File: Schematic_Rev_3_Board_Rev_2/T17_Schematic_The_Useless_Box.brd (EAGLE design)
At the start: 100 x 80 mm, 18 parts, among them U1 ATMEGA328P-AU

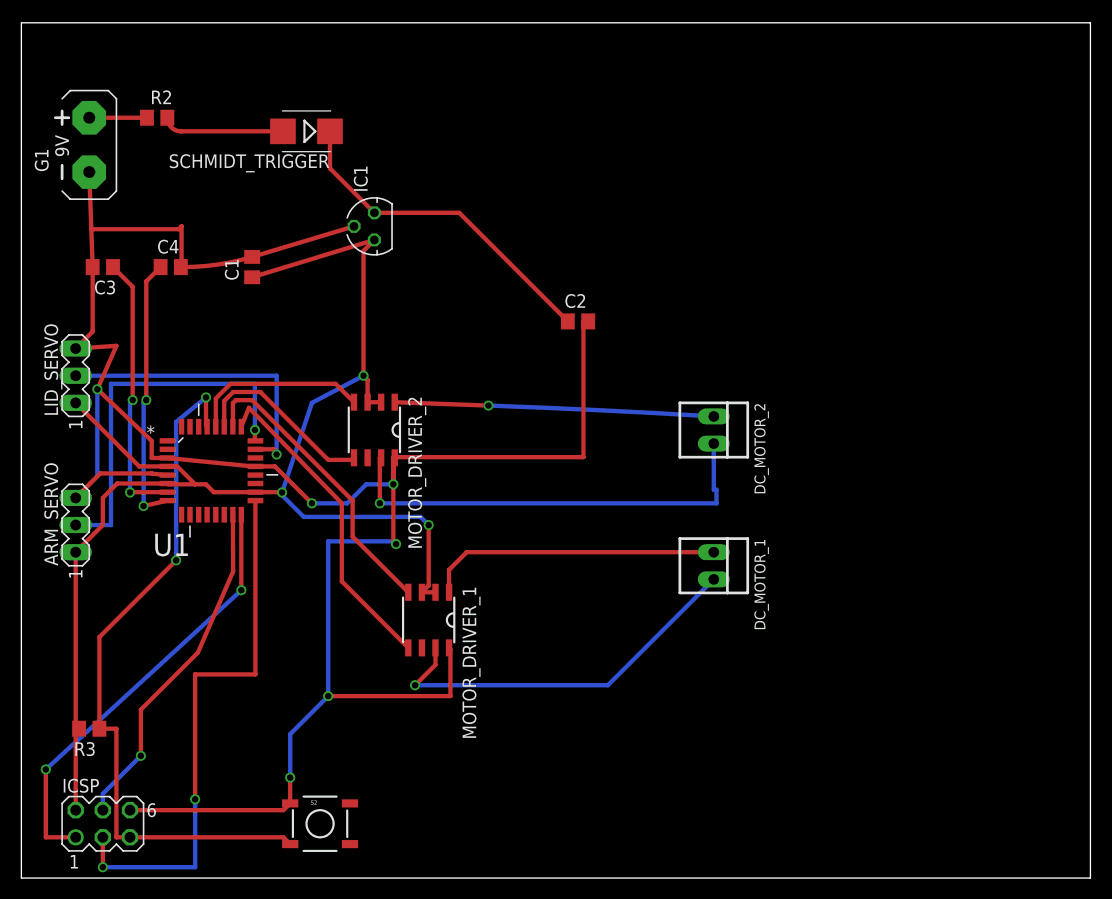
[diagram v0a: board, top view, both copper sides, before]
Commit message: ACTUALLY updating the schematics this time. Picture added for modification on the wiki.
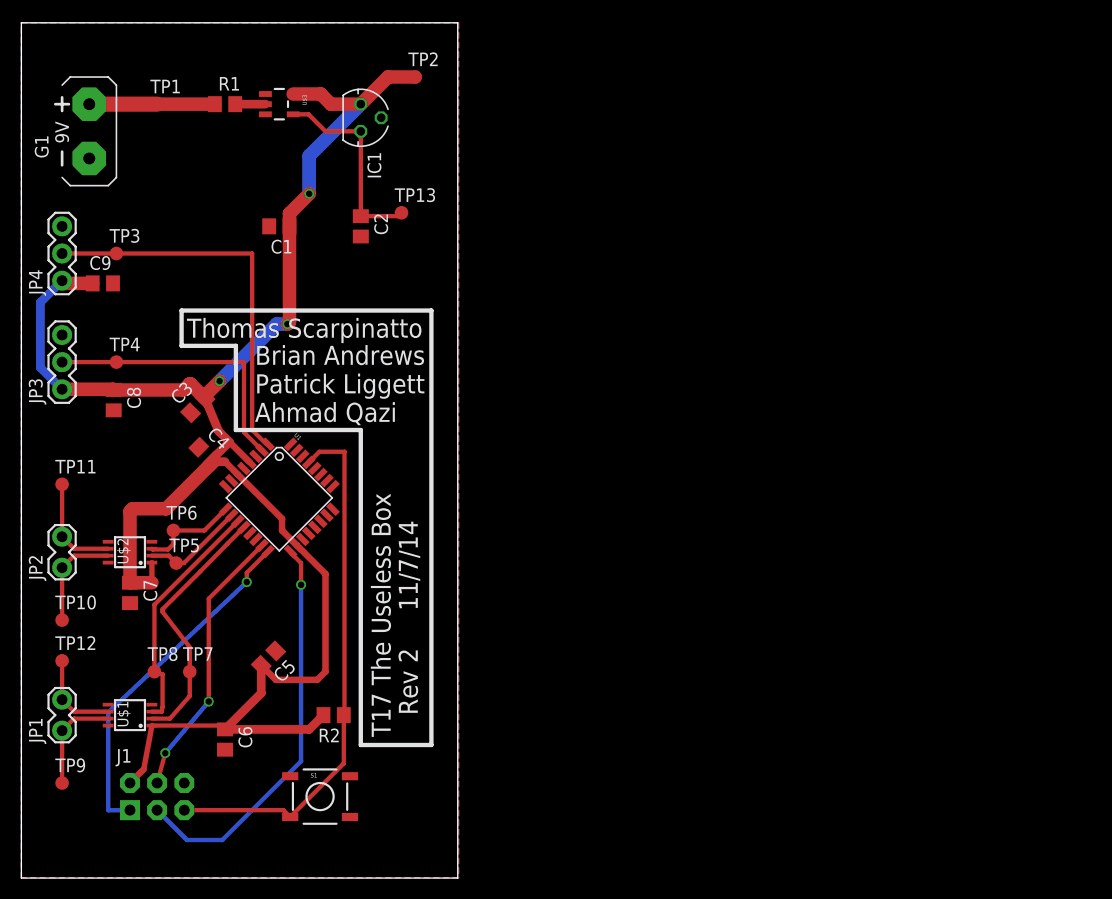
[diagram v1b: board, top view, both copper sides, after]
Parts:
- removed ARM_SERVO, LID_SERVO: (no value), con-lstb:MA03-1
- removed DC_MOTOR_1, DC_MOTOR_2: 22-23-2021, con-molex:22-23-2021
- removed ICSP: (no value), con-lstb:MA03-2
- removed MOTOR_DRIVER_1, MOTOR_DRIVER_2: BD6230F, rohm:SOP8
- removed R3: 10k, rcl:R0805
- removed S2: SWITCH-MOMENTARY-2SMD, SparkFun-Electromechanical:TACTILE-SWITCH-SMD
- removed SCHMIDT_TRIGGER: ES2D, diode:SMB
- added C5, C6, C7, C8, C9: 10nF, rcl:C0805
- added J1: AVR_SPI_PRG_6NS, SparkFun-Connectors:2X3-NS
- added JP1, JP2: M02LOCK, SparkFun-Connectors:1X02_LOCK
- added JP3: ARM_SERVO, SparkFun-Connectors:1X03
- added JP4: LID_SERVO, SparkFun-Connectors:1X03
- added R1: 0, rcl:R0805
- added S1: SWITCH-MOMENTARY-2SMD, SparkFun-Electromechanical:TACTILE-SWITCH-SMD
- added TP1, TP10, TP11, TP12, TP13, TP2, TP3, TP4, TP5, TP6, TP7, TP8, TP9: TPB1,27, testpad:B1,27
- added U$1, U$2: LB1938FA-AH, microchip-MCP125x-xxx:MSOP8
- added U$3: INVERTING_SCHMITT_TRIGGER, SparkFun-DigitalIC:SOT23-5
- R2: value 0 -> 10K
- U1: value ATMEGA328P-AU -> ATMEGA328P; device Atmel_By_element14_Batch_1-00:QFP80P900X900X120-32N -> SparkFun-DigitalIC:TQFP32-08
- moved R2 58.3 mm to (29.2, 15.2), turned to 180 degrees
- moved C2 22.2 mm to (31.8, 61.0), turned to 270 degrees
- moved C4 17.8 mm to (17.3, 39.6), turned to 315 degrees
- moved C3 15.7 mm to (16.5, 44.2), turned to 45 degrees
- moved IC1 10.2 mm to (31.8, 71.1), turned to 270 degrees
- moved U1 6.84 mm to (24.1, 35.6), turned to 315 degrees
- moved C1 4.58 mm to (24.1, 61.0), turned to 180 degrees
- moved G1 1.27 mm to (6.35, 69.8)
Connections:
- removed net +5V: ARM_SERVO.1, C1.1, IC1.OUT, ICSP.2, LID_SERVO.1, MOTOR_DRIVER_1.2, MOTOR_DRIVER_1.3, MOTOR_DRIVER_2.2, MOTOR_DRIVER_2.3, R3.2, U1.18, U1.4, U1.6
- removed net N$19: MOTOR_DRIVER_1.5, U1.25
- removed net N$21: MOTOR_DRIVER_2.5, U1.27
- removed net N$22: LID_SERVO.2, U1.23
- removed net N$23: ARM_SERVO.2, U1.24
- removed net N$24: DC_MOTOR_2.1, MOTOR_DRIVER_2.1
- removed net N$25: DC_MOTOR_1.1, MOTOR_DRIVER_1.1
- removed net N$26: DC_MOTOR_1.2, MOTOR_DRIVER_1.7
- removed net N$27: DC_MOTOR_2.2, MOTOR_DRIVER_2.7
- new net 5V: C1.1, C3.2, C4.2, C5.2, C6.1, C7.1, C8.1, C9.1, IC1.OUT, J1.2, JP3.1, JP4.1, R2.2, TP2.TP, U$1.1, U$2.1, U$3.5, U1.18, U1.4, U1.6
- new net N$10: JP4.2, TP3.TP, U1.1
- new net N$13: TP5.TP, U$2.2, U1.10
- new net N$16: J1.5, R2.1, S1.3, U1.29
- new net N$2: JP1.1, TP9.TP, U$1.7
- new net N$4: JP2.2, TP11.TP, U$2.6
- new net N$5: JP2.1, TP10.TP, U$2.7
- net GND: now also C3.1, C4.1, C5.1, C6.2, C7.2, C8.2, C9.2, J1.6, JP3.3, JP4.3, S1.1, U$1.4, U$1.8, U$2.4, U$2.8, U$3.3; no longer ARM_SERVO.3, C3.2, C4.2, ICSP.6, LID_SERVO.3, MOTOR_DRIVER_1.8, MOTOR_DRIVER_2.8, S2.1
- net N$1: now also TP7.TP, U$1.2, U1.12; no longer ICSP.3, U1.17
- net N$11: now also R1.2, U$3.2; no longer C3.1, U1.7
- net N$12: now also G1.+, R1.1, TP1.TP; no longer ICSP.5, R3.1, S2.3, U1.29
- net N$14: now also J1.3, U1.17; no longer C4.1, U1.8
- net N$18: now also J1.1, U1.16; no longer MOTOR_DRIVER_1.4, U1.26
- net N$20: now also TP6.TP, U$2.3, U1.9; no longer MOTOR_DRIVER_2.4, U1.28
- net N$3: now also JP1.2, TP12.TP, U$1.6; no longer C2.1, IC1.IN, SCHMIDT_TRIGGER.C
- net N$6: now also TP8.TP, U$1.3, U1.11; no longer R2.2, SCHMIDT_TRIGGER.A
- net N$7: now also J1.4, U1.15; no longer G1.+, R2.1
- net N$8: now also JP3.2, TP4.TP, U1.2; no longer ICSP.1, U1.16
- net N$9: now also C2.1, IC1.IN, TP13.TP, U$3.4; no longer ICSP.4, U1.15
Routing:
- net GND: track 214.0 -> 0.00 mm, vias 6 -> 0
- net 5V: track 0.00 -> 168.3 mm, vias 0 -> 3
- net +5V: track 129.0 -> 0.00 mm, vias 3 -> 0
- net N$12: track 66.3 -> 11.8 mm, vias 2 -> 0
- net N$16: track 0.00 -> 50.2 mm
- net N$27: track 41.7 -> 0.00 mm, vias 1 -> 0
- net N$26: track 36.3 -> 0.00 mm, vias 1 -> 0
- net N$10: track 0.00 -> 36.2 mm
- net N$23: track 35.3 -> 0.00 mm, vias 1 -> 0
- net N$19: track 30.5 -> 0.00 mm
- net N$24: track 29.9 -> 0.00 mm, vias 1 -> 0
- net N$22: track 28.4 -> 0.00 mm, vias 1 -> 0
- net N$25: track 27.5 -> 0.00 mm
- net N$1: track 51.4 -> 24.3 mm, vias 2 -> 0
- net N$3: track 31.6 -> 8.40 mm
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- added copper zone on layer 1, net GND
- added copper zone on layer 16, net GND
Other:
- board size 100 x 80 mm -> 40.8 x 80 mm
- board text added: "Brian Andrews Patrick Liggett Ahmad Qazi"
- board text added: "Rev 2 11/7/14"
- board text added: "T17 The Useless Box"
- board text added: "Thomas Scarpinatto"

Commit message: Added mounting holes and ground plane staples
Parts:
- renumbered IC1 to 78L05
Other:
- board text added: "Rev 3 11/8/14"
- board text removed: "Rev 2 11/7/14"
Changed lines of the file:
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@@
 <layer number="43" name="vRestrict" color="2" fill="10" visible="yes" active="yes"/>
 <layer number="44" name="Drills" color="7" fill="1" visible="no" active="yes"/>
-<layer number="45" name="Holes" color="7" fill="1" visible="no" active="yes"/>
+<layer number="45" name="Holes" color="7" fill="1" visible="yes" active="yes"/>
 <layer number="46" name="Milling" color="3" fill="1" visible="no" active="yes"/>
 <layer number="47" name="Measures" color="7" fill="1" visible="no" active="yes"/>
@@
 <wire x1="38.354" y1="53.086" x2="14.986" y2="53.086" width="0.4064" layer="21"/>
 <text x="34.544" y="13.208" size="1.778" layer="21" rot="R90">T17 The Useless Box</text>
-<text x="37.084" y="15.24" size="1.778" layer="21" rot="R90">Rev 2     11/7/14</text>
+<text x="37.084" y="15.24" size="1.778" layer="21" rot="R90">Rev 3     11/8/14</text>
 <wire x1="14.986" y1="53.086" x2="14.986" y2="49.784" width="0.4064" layer="21"/>
 <wire x1="14.986" y1="49.784" x2="20.066" y2="49.784" width="0.4064" layer="21"/>
@@
 Ahmad Qazi</text>
 <text x="15.494" y="50.546" size="1.778" layer="21">Thomas Scarpinatto</text>
+<hole x="2.794" y="76.962" drill="2.8"/>
+<hole x="30.988" y="76.708" drill="2.8"/>
+<hole x="37.084" y="3.048" drill="2.8"/>
+<hole x="3.048" y="3.302" drill="2.8"/>
 </plain>
 <attributes>
@@
 <element name="C7" library="rcl" package="C0805" value="10nF" x="10.16" y="26.67" rot="R270"/>
 <element name="G1" library="battery" package="AB9V" value="AB9V" x="6.35" y="69.85"/>
-<element name="IC1" library="v-reg" package="78LXX" value="" x="31.75" y="71.12" rot="R270"/>
+<element name="78L05" library="v-reg" package="78LXX" value="" x="31.75" y="71.12" rot="R270"/>
 <element name="J1" library="SparkFun-Connectors" package="2X3-NS" value="AVR_SPI_PRG_6NS" x="12.7" y="7.62"/>
 <element name="JP1" library="SparkFun-Connectors" package="1X02_LOCK" value="M02LOCK" x="3.81" y="13.97" rot="R90"/>
@@
 <contactref element="U1" pad="5"/>
 <contactref element="C1" pad="2"/>
-<contactref element="IC1" pad="GND"/>
+<contactref element="78L05" pad="GND"/>
 <contactref element="C2" pad="2"/>
 <contactref element="U$3" pad="3"/>
@@
 <vertex x="40.894" y="0"/>
 </polygon>
-<wire x1="12.21" y1="31.455" x2="8.11" y2="29.505" width="0" layer="19" extent="1-1"/>
+<via x="29.21" y="2.794" extent="1-16" drill="0.5"/>
+<via x="20.574" y="8.89" extent="1-16" drill="0.5"/>
+<via x="4.572" y="6.604" extent="1-16" drill="0.5"/>
+<via x="24.384" y="16.256" extent="1-16" drill="0.5"/>
+<via x="36.576" y="23.622" extent="1-16" drill="0.5"/>
+<via x="22.098" y="24.384" extent="1-16" drill="0.5"/>
+<via x="8.382" y="22.606" extent="1-16" drill="0.5"/>
+<via x="35.306" y="39.878" extent="1-16" drill="0.5"/>
+<via x="10.16" y="40.894" extent="1-16" drill="0.5"/>
+<via x="14.732" y="54.61" extent="1-16" drill="0.5"/>
+<via x="34.798" y="55.88" extent="1-16" drill="0.5"/>
+<via x="15.24" y="65.278" extent="1-16" drill="0.5"/>
+<via x="38.354" y="70.866" extent="1-16" drill="0.5"/>
+<via x="15.748" y="77.47" extent="1-16" drill="0.5"/>
+<via x="1.778" y="64.516" extent="1-16" drill="0.5"/>
 </signal>
 <signal name="N$2">
@@
 <signal name="N$9">
 <contactref element="U$3" pad="4"/>
-<contactref element="IC1" pad="IN"/>
+<contactref element="78L05" pad="IN"/>
 <contactref element="C2" pad="1"/>
 <contactref element="TP13" pad="TP"/>
@@
 <contactref element="U$1" pad="1"/>
 <contactref element="C7" pad="1"/>
-<contactref element="IC1" pad="OUT"/>
+<contactref element="78L05" pad="OUT"/>
 <contactref element="C1" pad="1"/>
 <contactref element="U$3" pad="5"/>

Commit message: submittable board?
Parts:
- removed 78L05: (no value), v-reg:78LXX
- removed G1: AB9V, battery:AB9V
- removed TP13: TPB1,27, testpad:B1,27
- removed U$3: INVERTING_SCHMITT_TRIGGER, SparkFun-DigitalIC:SOT23-5
- added 9V-BATTERY-CLIP: M02LOCK, SparkFun-Connectors:1X02_LOCK
- added C10, C11: 22pF, rcl:C0805
- added IC1: (no value), SparkFun-PowerIC:TO-220-ALT
- added JP5: (no value), SparkFun-Connectors:1X06_NO_SILK
- added Q1: 16kHz, special:QS
- added R3, R4, R5, R6: 10K, rcl:R0805
- C6, C7: value 10nF -> 10uF
- moved TP2 23.3 mm to (14.7, 67.6)
- moved C2 18.6 mm to (22.4, 77.0), turned to 0 degrees
- moved C9 13.0 mm to (7.62, 68.6), turned to 90 degrees
- moved C3 11.2 mm to (13.0, 54.9), turned to 0 degrees
- moved C4 10.7 mm to (12.2, 49.0), turned to 270 degrees
- moved TP4 10.2 mm to (3.56, 56.9)
- moved C1 9.12 mm to (15.2, 63.0)
- moved JP3 8.39 mm to (3.56, 54.1), turned to 0 degrees
- moved JP4 8.39 mm to (3.56, 64.3), turned to 0 degrees
- moved TP3 5.62 mm to (3.56, 60.2)
- moved C8 4.72 mm to (5.84, 48.5), turned to 180 degrees
- moved R1 4.06 mm to (15.0, 72.4)
- moved C7 1.78 mm to (10.2, 24.9)
- moved TP1 1.27 mm to (11.4, 72.4)
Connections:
- new net N$15: JP5.4, U1.31
- new net N$17: C11.2, Q1.1, U1.8
- new net N$19: C10.2, Q1.2, U1.7
- net 5V: now also IC1.OUT, JP3.2, JP4.2; no longer 78L05.OUT, JP3.1, JP4.1, U$3.5
- net GND: now also 9V-BATTERY-CLIP.1, C10.1, C11.1, IC1.GND, JP5.1, R3.1, R4.1, R5.1, R6.1; no longer 78L05.GND, G1.-, U$3.3
- net N$1: now also R6.2
- net N$10: now also JP4.1; no longer JP4.2
- net N$11: now also C2.1, IC1.IN; no longer U$3.2
- net N$12: now also 9V-BATTERY-CLIP.2; no longer G1.+
- net N$13: now also R3.2
- net N$20: now also R4.2
- net N$6: now also R5.2
- net N$8: now also JP3.1; no longer JP3.2
- net N$9: now also JP5.5, U1.30; no longer 78L05.IN, C2.1, TP13.TP, U$3.4
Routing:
- net 5V: track 168.3 -> 290.5 mm
- net N$17: track 0.00 -> 37.6 mm, vias 0 -> 1
- net N$19: track 0.00 -> 22.5 mm, vias 0 -> 1
- net N$15: track 0.00 -> 22.1 mm
- net N$13: track 9.61 -> 22.4 mm, vias 0 -> 2
- net N$8: track 26.0 -> 37.6 mm
- net N$1: track 24.3 -> 33.8 mm
- net N$11: track 2.83 -> 10.0 mm
- net N$12: track 11.8 -> 5.98 mm
- net N$10: track 36.2 -> 41.6 mm
- net GND: track 0.00 -> 4.75 mm, vias 15 -> 20
- net N$9: track 18.9 -> 23.4 mm
- net N$20: track 9.24 -> 12.9 mm
- net N$6: track 22.5 -> 25.2 mm
- net N$16: track 50.2 -> 49.5 mm
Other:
- board size 40.8 x 80 mm -> 41.1 x 80 mm

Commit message: Adding the final ckt design
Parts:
- added C12: 10nF, rcl:C0805
- added TOGGLE: M02LOCK, SparkFun-Connectors:1X02_LOCK
- Q1: value 16kHz -> 16MHz
- moved S1 6.14 mm to (21.8, 8.38)
- renumbered JP1 to R-MOTOR, JP2 to L-MOTOR, JP5 to PROGRAMMING
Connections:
- new net N$21: TOGGLE.2, U1.24
- net 5V: now also C12.1, TOGGLE.1
- net GND: now also C12.2
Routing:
- net N$21: track 0.00 -> 28.6 mm, vias 0 -> 1
- net N$16: track 49.5 -> 55.0 mm
- net 5V: track 290.5 -> 292.6 mm, vias 3 -> 4
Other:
- board text added: "T. Scarpinatto"
- board text removed: "Thomas Scarpinatto"
